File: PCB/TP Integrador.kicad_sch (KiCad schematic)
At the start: 28 parts, among them Q1 BC547C, Q10 BC547C, Q2 2N3019, Q3 D45H11, Q4 BC547C, Q5 BC557C, Q6 BC557C, Q7 BC547C, Q8 BC557C, Q9 BC547C

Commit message: Upate PCB
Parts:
- added C1: C, Capacitor_THT:CP_Radial_D4.0mm_P1.50mm, symbol Device:C
- added Q11: BC547C, Package_TO_SOT_THT:TO-92_Inline_Wide, symbol ltspice:npn
- added RL2: 50, Resistor_THT:R_Axial_DIN0207_L6.3mm_D2.5mm_P7.62mm_Horizontal, symbol ltspice:res
- added RL3, RL4: 50, Resistor_THT:R_Axial_DIN0207_L6.3mm_D2.5mm_P5.08mm_Vertical, symbol ltspice:res
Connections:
- net GND: now also C1.2, RL4.1
- net vo: now also C1.1, Q11.3 (E), RL2.2; no longer Q2.3 (E), Q3.1 (C)
- net at Q2.2 (B), Q7.1 (C), Q8.1 (C): now also Q11.1 (C)
- new net: Q11.2 (B), RL3.1, RL4.2
- new net: Q2.3 (E), Q3.1 (C), RL2.1, RL3.2
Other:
- note removed: "-100*(V(vo)*I(RL))/(V(vi)*I(Vi))"
- note removed: ".dc Vi 0 8 .param RL 3.33 .meas DC VoEspMin FIND V(vo) AT 6.6 .meas DC VoEspMed FIND V(vo) AT 6.8 .meas DC VoEspMax FIND V(vo) AT 7 .meas DC VoError PARAM ((VoEspMin + VoEspMed + VoEspMax)/3 - 5)"
- note removed: ".dc Vi 0 8 .param RL=3.33 .meas DC Vol1rl FIND V(vo) AT=6.6 .meas DC Vol2rl FIND V(vo) AT=7 .meas DC RegLin PARAM ((Vol2rl - Vol1rl) / 0.4)"
- note removed: ".dc Vi 6.6 7 .param RL=3.33"
- note removed: ".dc Vi 6.6 7 .param RL=3.33 .meas DC VoEnc FIND V(vo) AT 6.8 .meas DC LDO PARAM (6.6 - VoEnc)"
- note removed: ".model TBJ-NPN-1 NPN(IS=4.679E-14 NF=1.01 ISE=2.642E-15 NE=1.581 BF={BETA} IKF=0.1371 VAF=52.64 NR=1.019 ISC=2.337E-14 NC=1.164 BR=11.57 IKR=0.1144 VAR=364.5 RB=1 IRB=1.00E-06 RBM=1 RE=0.2598 RC=1 XTB=0 EG=1.11 XTI=3 CJE=1.229E-11 VJE=0.5591 MJE=0.3385 TF=4.689E-10 XTF=160 VTF=2.828 ITF=0.8842 PTF=0 CJC=4.42E-12 VJC=0.1994 MJC=0.2782 XCJC=0.6193 TR=1.00E-32 CJS=0 VJS=0.75 MJS=0.333 FC=0.7936 Vceo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"
- note removed: ".op .step param RL 3.33 500 50 .meas OP Vo1rc FIND V(vo) AT 500 .meas OP Vo2rc FIND V(vo) AT 3.33 .meas OP Io1rc FIND I(RL) AT 500 .meas OP Io2rc FIND I(RL) AT 3.33 .meas OP RegCar PARAM (-(Vo2rc - Vo1rc) / (Io2rc - Io1rc) )"
- note removed: ".param BETA 458.7"
- note removed: ".param RB1=51"
- note removed: ".param RB2=1.8k"
- note removed: ".param RC1=510"
- note removed: ".param RC2=510"
- note removed: ".param RE=390"
- note removed: ".param VREF=1.56"
- note removed: ".param Vi=6.8"
- note removed: ".step param BETA list 420 520 800"
- note removed: ".step param RB1 list 46 56"
- note removed: ".step param RB2 1.5k 3k 500"
- note removed: ".step param RC 100 1500 100"
- note removed: ".step param RC1 list 460 510 560"
- note removed: ".step param RC2 list 460 510 560"
- note removed: ".step param RE list 250 500 1k"
- note removed: ".step param RL 3.33 500 1"
- note removed: ".step param VREF 1.5 1.6 0.01"
- note removed: "Eficiencia"
- note removed: "Generador"
- note removed: "LDO"
- note removed: "Parametros generales"
- note removed: "Pruebas"
- note removed: "Regulacion de carga"
- note removed: "Regulacion de linea"
- note removed: "Tensión de salida"
- note removed: "Usar un potenciometro en el diseño final"
- moved on the sheet: RL1

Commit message: Update checkpoint 2
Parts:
- removed Q2: 2N3019, Package_TO_SOT_THT:TO-39-3, symbol ltspice:npn
- removed Q3: D45H11, Package_TO_SOT_THT:TO-220-3_Vertical, symbol ltspice:pnp
- removed Q7: BC547C, Package_TO_SOT_THT:TO-92_Inline_Wide, symbol ltspice:npn
- removed Q8: BC557C, Package_TO_SOT_THT:TO-92_Inline_Wide, symbol ltspice:pnp
- removed RB1: 51, Resistor_THT:R_Axial_DIN0207_L6.3mm_D2.5mm_P7.62mm_Horizontal, symbol ltspice:res
- removed RB2: 1.8k, Resistor_THT:R_Axial_DIN0207_L6.3mm_D2.5mm_P7.62mm_Horizontal, symbol ltspice:res
- removed VREF1: 1.56, TerminalBlock_Phoenix:TerminalBlock_Phoenix_MKDS-1,5-2-5.08_1x02_P5.08mm_Horizontal, symbol ltspice:voltage
- added CComp1: 12n, Capacitor_THT:CP_Radial_D4.0mm_P1.50mm, symbol Device:C
- added JP3, JP4: Jumper_2_Bridged, TestPoint:TestPoint_2Pads_Pitch5.08mm_Drill1.3mm, symbol Jumper:Jumper_2_Bridged
- added Q2: 2SB631, Package_TO_SOT_THT:TO-126-3_Vertical, symbol Transistor_BJT:2SB631
- added Q3: BC547, Package_TO_SOT_THT:TO-92_Inline_Wide, symbol Transistor_BJT:BC547
- added R8: 2200, Resistor_THT:R_Axial_DIN0207_L6.3mm_D2.5mm_P7.62mm_Horizontal, symbol ltspice:res
- added U1: TL431D, Package_TO_SOT_THT:TO-92_Inline_Wide, symbol Reference_Voltage:TL431D
- CL1: renamed from C1; value C -> 2.2u
- RD1: value 2.2k -> 1k
- RS1: renamed from RL2; value 50 -> 2.2
- renumbered RL3 to RP1, RL4 to RP2
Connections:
- net GND: now also CComp1.2, U1.2 (A), U1.3 (A), U1.6 (A), U1.7 (A)
- net vi: now also JP2.1 (A), R8.1
- net vo: now also JP4.2 (B); no longer Q11.3 (E), RS1.2
- net at Q11.1 (C): now also Q4.1 (C), Q5.1 (C), CComp1.1, Q3.2 (B)
- net at RP1.2, RS1.1: now also JP3.2 (B)
- net at Q5.2 (B), Q6.2 (B): now also Q1.1 (C), Q6.1 (C); no longer Q4.1 (C), Q5.1 (C)
- net at JP2.2 (B): now also Q2.1 (E)
- net vref: no longer names the net of Q1.2 (B), R1.1
- net vref: now also R8.2, U1.1 (K), U1.8 (REF)
- new net: JP3.1 (A), Q2.2 (C), Q3.3 (E)
- new net: Q2.3 (B), Q3.1 (C)
- new net: JP4.1 (A), Q11.3 (E), RS1.2
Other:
- moved on the sheet: JP2, VI1

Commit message: Edit Checkpoint 2
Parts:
- added JP5, JP6, JP7, JP8: Jumper_2_Bridged, TestPoint:TestPoint_2Pads_Pitch5.08mm_Drill1.3mm, symbol Jumper:Jumper_2_Bridged
- CComp1, CL1: footprint Capacitor_THT:CP_Radial_D4.0mm_P1.50mm -> Capacitor_THT:CP_Radial_D8.0mm_P3.80mm
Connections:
- net at CComp1.1, Q11.1 (C), Q3.2 (B): now also JP6.2 (B); no longer Q4.1 (C), Q5.1 (C)
- net at RP1.1, RP2.2: now also JP7.1 (A); no longer Q11.2 (B)
- net at R8.2, U1.1 (K), U1.8 (REF): now also JP8.1 (A); no longer Q1.2 (B), R1.1
- net at Q1.3 (E), Q9.1 (C): now also JP5.1 (A); no longer Q4.3 (E)
- new net: JP8.2 (B), Q1.2 (B), R1.1
- new net: JP7.2 (B), Q11.2 (B)
- new net: JP6.1 (A), Q4.1 (C), Q5.1 (C)
- new net: JP5.2 (B), Q4.3 (E)
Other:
- note removed: "Amplificador"
- note removed: "Realimentador"
- moved on the sheet: CComp1, CL1, H4, JP1, JP2, JP3, JP4, Q11, Q2, Q3, RD1, RD2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

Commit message: Falta el disipador!!!
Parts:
- removed CL1: 2.2u, Capacitor_THT:CP_Radial_D8.0mm_P3.80mm, symbol Device:C
- removed RL1: 50, Resistor_THT:R_Axial_DIN0207_L6.3mm_D2.5mm_P7.62mm_Horizontal, symbol ltspice:res
- added CL1, RL1: Jumper_2_Bridged, TestPoint:TestPoint_2Pads_Pitch5.08mm_Drill1.3mm, symbol Jumper:Jumper_2_Bridged
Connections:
- net GND: now also CL1.2 (B), RL1.2 (B)
- net vo: now also CL1.1 (A), RL1.1 (A)

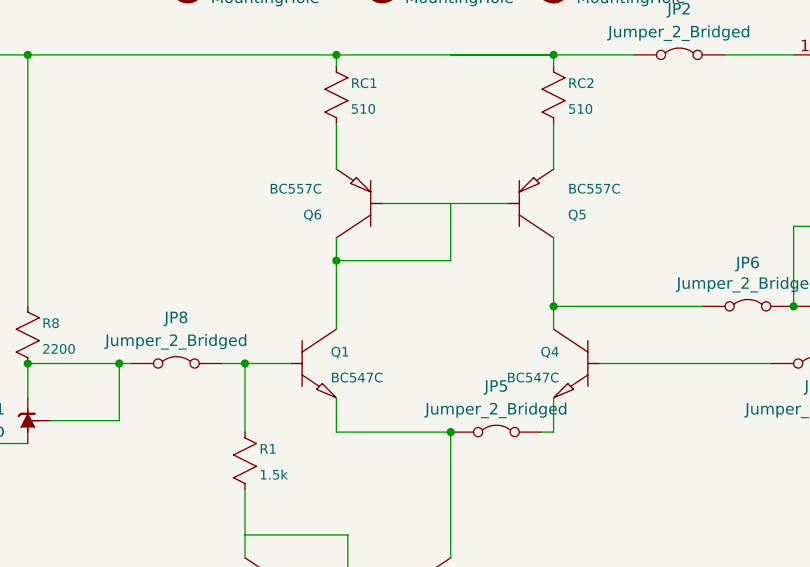
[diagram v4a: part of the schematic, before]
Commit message: Edit Rs, no falta el disipador!!
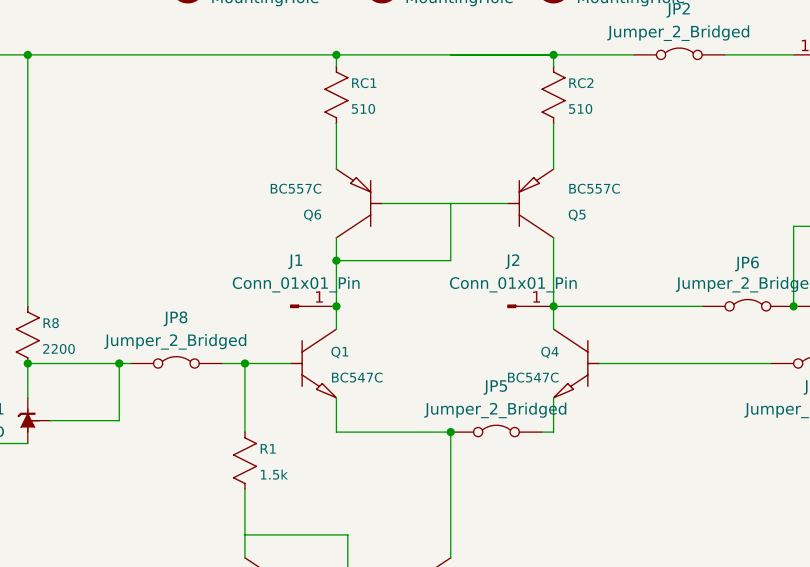
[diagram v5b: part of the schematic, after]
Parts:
- added J1, J2: Conn_01x01_Pin, Connector_PinHeader_1.00mm:PinHeader_1x01_P1.00mm_Vertical, symbol Connector:Conn_01x01_Pin
- RS1: footprint Resistor_THT:R_Axial_DIN0207_L6.3mm_D2.5mm_P7.62mm_Horizontal -> Resistor_THT:R_Axial_DIN0617_L17.0mm_D6.0mm_P20.32mm_Horizontal
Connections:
- net at JP6.1 (A), Q4.1 (C), Q5.1 (C): now also J2.1 (Pin_1)
- net at Q1.1 (C), Q5.2 (B), Q6.1 (C)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: now also J1.1 (Pin_1)
